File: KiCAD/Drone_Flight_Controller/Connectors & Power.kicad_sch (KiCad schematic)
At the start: 54 parts, among them J201 Conn_01x04, J205 XT60, J207 Conn_01x05, Q201 BC846C, Q202 BC856C, Q203 BC846C, Q204 BC856C, Q205 BC846C, Q206 BC856C, Q207 BC846C, Q208 BC856C, U201 AS358, U202 AS358, U205 AS358

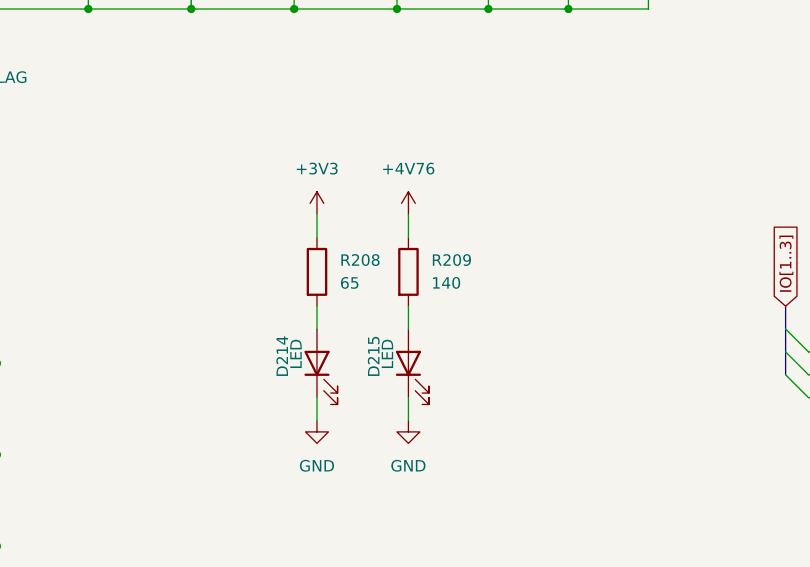
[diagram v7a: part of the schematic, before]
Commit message: Add footprints for LED protection resistors
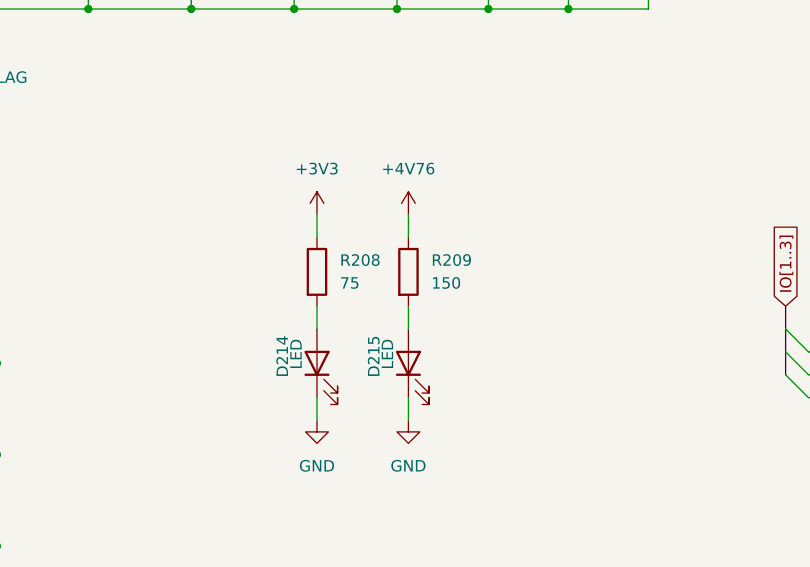
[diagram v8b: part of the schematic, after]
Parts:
- R208: value 65 -> 75; footprint (none) -> Resistor_SMD:R_0805_2012Metric_Pad1.20x1.40mm_HandSolder; Link (none) -> https://eu.mouser.com/ProductDetail/YAGEO/RC0805FR-0775RP?q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
- R209: value 140 -> 150; footprint (none) -> Resistor_SMD:R_0805_2012Metric_Pad1.20x1.40mm_HandSolder; Link (none) -> https://eu.mouser.com/ProductDetail/YAGEO/RE0805DRE07150RL?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
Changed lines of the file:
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@@
 			)
 		)
-		(property "Value" "140"
+		(property "Value" "150"
 			(at 91.44 149.8599 0)
 			(effects
@@
 			)
 		)
-		(property "Footprint" ""
+		(property "Footprint" "Resistor_SMD:R_0805_2012Metric_Pad1.20x1.40mm_HandSolder"
 			(at 87.122 148.59 90)
 			(effects
@@
 			)
 		)
-		(property "Datasheet" "~"
+		(property "Datasheet" "https://eu.mouser.com/datasheet/3/508/1/pyu-re_105_rohs_l.pdf"
 			(at 88.9 148.59 0)
 			(effects
@@
 			)
 		)
+		(property "Link" "https://eu.mouser.com/ProductDetail/YAGEO/RE0805DRE07150RL?qs=sGAEpiMZZMtlubZbdhIBIKm0gsRX2fVk4SNsBClYUIM%3D"
+			(at 88.9 148.59 0)
+			(effects
+				(font
+					(size 1.27 1.27)
+				)
+				(hide yes)
+			)
+		)
 		(pin "2"
 		)
@@
 			)
 		)
-		(property "Value" "65"
+		(property "Value" "75"
 			(at 81.28 149.8599 0)
 			(effects
@@
 			)
 		)
-		(property "Footprint" ""
+		(property "Footprint" "Resistor_SMD:R_0805_2012Metric_Pad1.20x1.40mm_HandSolder"
 			(at 76.962 148.59 90)
 			(effects
@@
 			)
 		)
-		(property "Datasheet" "~"
+		(property "Datasheet" "https://eu.mouser.com/datasheet/3/508/1/pyu-rc_51_rohs_p.pdf"
 			(at 78.74 148.59 0)
 			(effects
@@
 			(at 78.74 148.59 0)
 			(effects
+				(font
+					(size 1.27 1.27)
+				)
+				(hide yes)
+			)
+		)
+		(property "Link" "https://eu.mouser.com/ProductDetail/YAGEO/RC0805FR-0775RP?qs=sGAEpiMZZMtlubZbdhIBIEgN9MQql2m6PtgO4vXfRRc%3D"
+			(at 78.74 148.59 0)
+			(effects
